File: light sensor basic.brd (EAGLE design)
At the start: 83.2 x 57.8 mm, 1 part

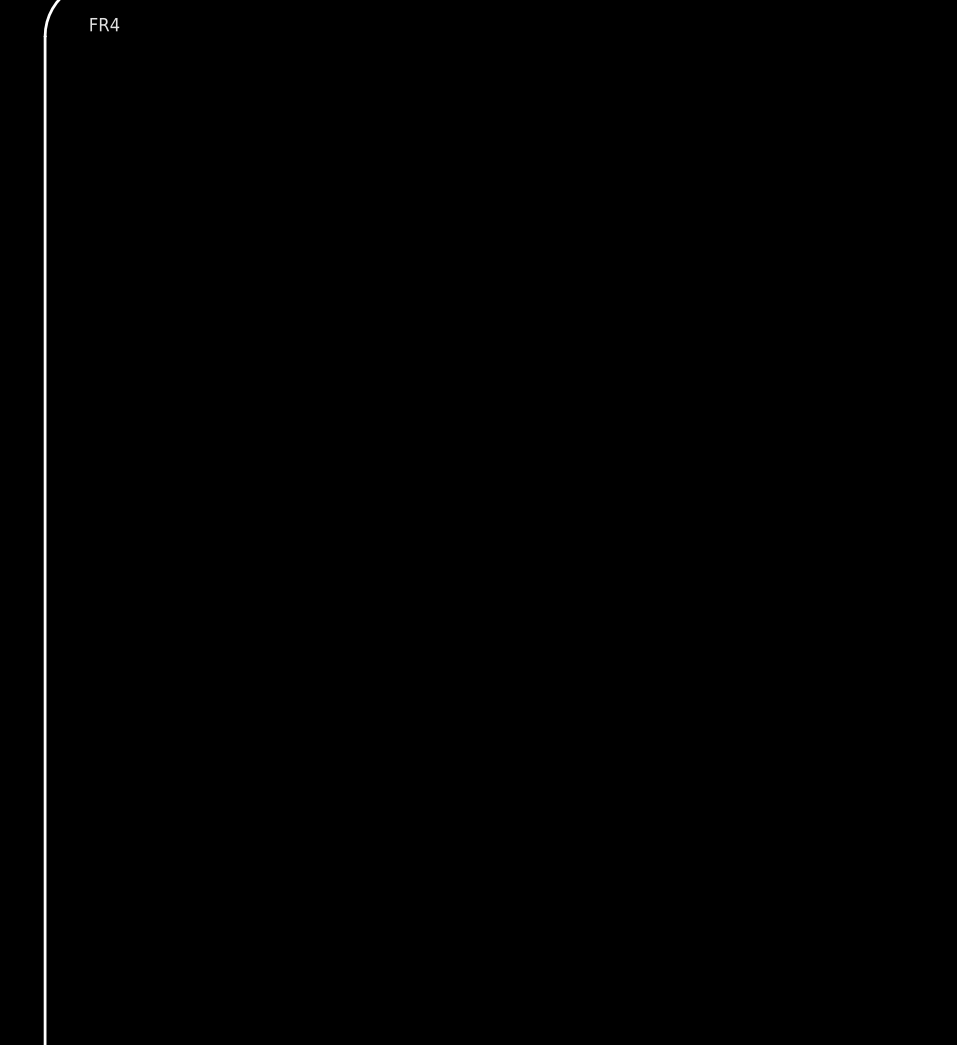
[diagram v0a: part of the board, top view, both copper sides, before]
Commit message: Update light sensor basic.brd
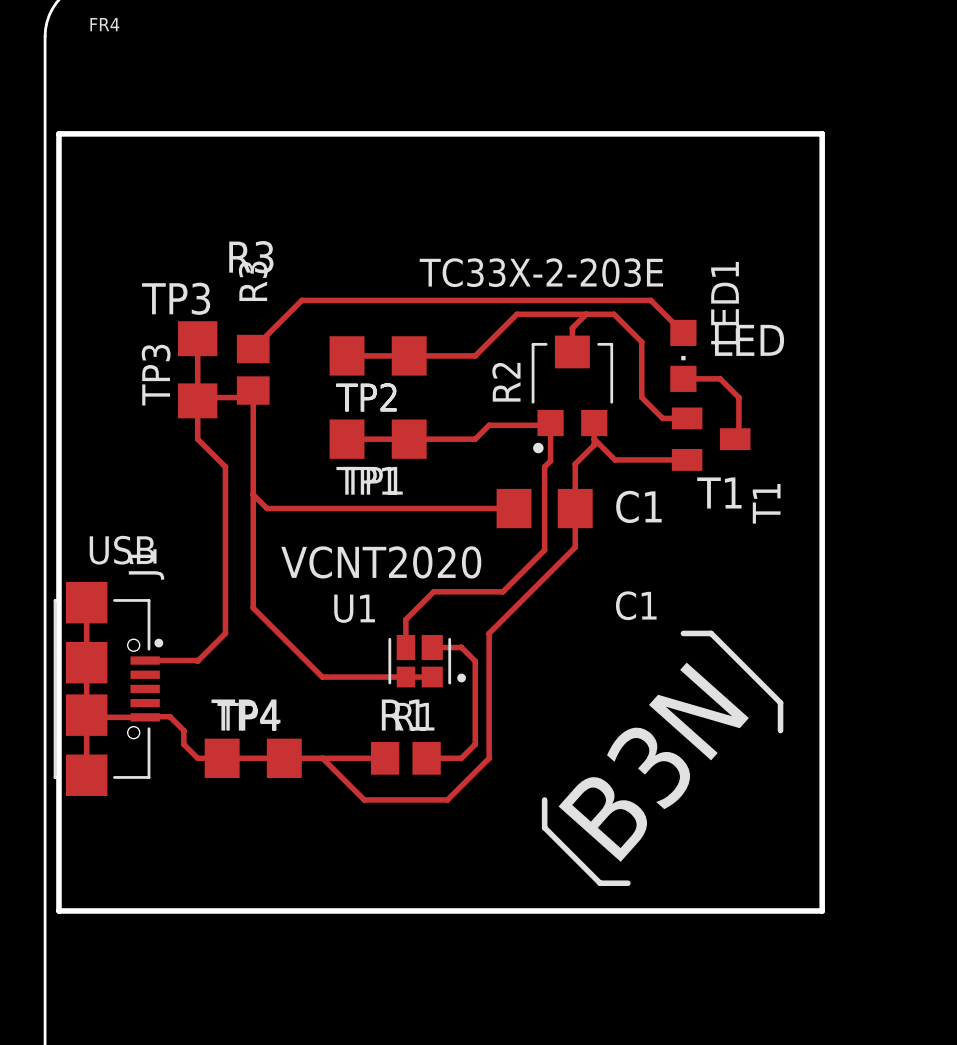
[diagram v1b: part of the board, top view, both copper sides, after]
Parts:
- added C1: 0.1 µF, rcl:C1206
- added J1: UJ2-MIBH-G-SMT-TR, UJ2-MIBH-G-SMT-TR:CUI_UJ2-MIBH-G-SMT-TR
- added LED1: (no value), led:CHIPLED_0805
- added R1: 82, rcl:R0805
- added R2: TC33X-2-203E, TC33X-2-203E:TRIM_TC33X-2-203E
- added R3: 150, rcl:R0805
- added T1: (no value), transistor:SOT23-BEC
- added TP1, TP2, TP3, TP4: (no value), rcl:R1206
- added U1: VCNT2020, VCNT2020:XDCR_VCNT2020
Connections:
- new net 0: C1.2, J1.5, J1.S1, J1.S2, J1.S3, J1.S4, R1.1, R2.3, T1.E, TP4.1, TP4.2
- new net N$1: R2.2, T1.B, TP2.1, TP2.2
- new net N$2: R1.2, U1.2
- new net N$3: LED1.C, T1.C
- new net N$5: R2.1, TP1.1, TP1.2, U1.4
- new net N$8: LED1.A, R3.1
- new net VCC: C1.1, J1.1, R3.2, TP3.1, TP3.2, U1.1, U1.3
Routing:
- net 0: track 0.00 -> 54.1 mm
- net VCC: track 0.00 -> 52.5 mm
- net N$5: track 0.00 -> 24.5 mm
- net N$1: track 0.00 -> 21.8 mm
- net N$8: track 0.00 -> 21.2 mm
- net N$2: track 0.00 -> 8.54 mm
- net N$3: track 0.00 -> 4.97 mm
- added copper zone on layer 1, net GND
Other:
- board text added: "B3N"
- board text added: "C1"
- board text added: "LED"
- board text added: "R1"
- board text added: "R3"
- board text added: "T1"
- board text added: "TC33X-2-203E"
- board text added: "TP1"
- board text added: "TP2"
- board text added: "TP3"
- board text added: "TP4"
- board text added: "USB"
- board text added: "VCNT2020"
